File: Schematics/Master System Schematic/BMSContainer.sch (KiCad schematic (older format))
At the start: 2 parts, among them U1 OrionBMS2v2, U2 OrionThermExp

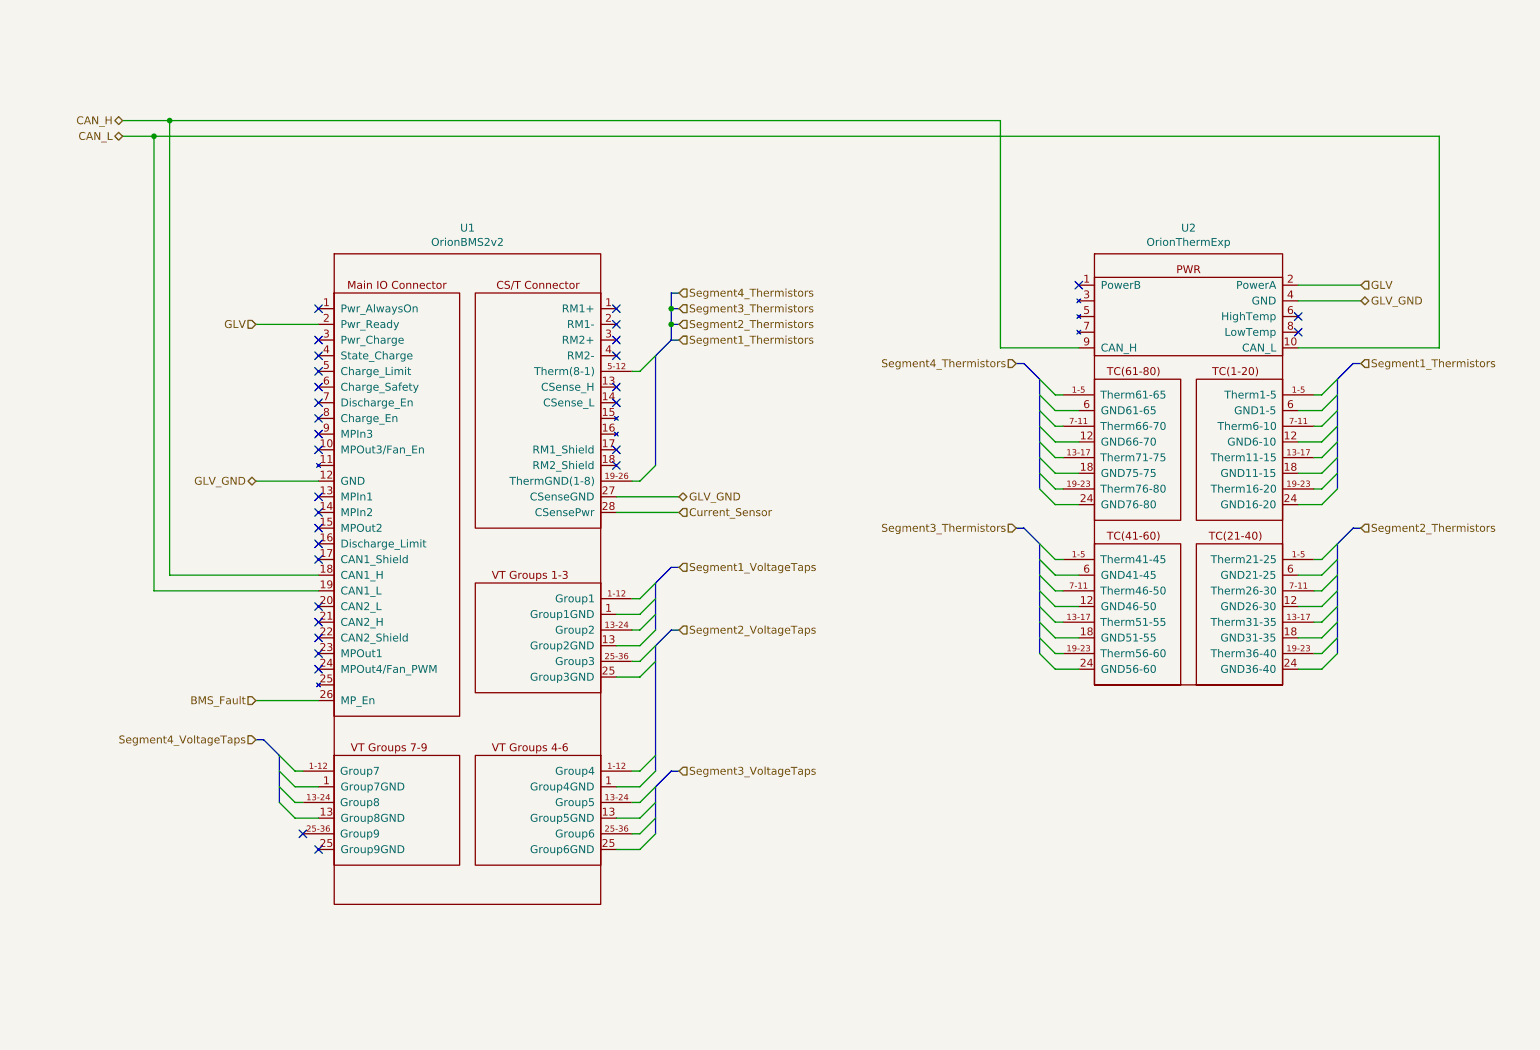
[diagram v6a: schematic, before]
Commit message: Additional corrections
>Moved GLV+ and GLV_GND pins to indicate single connections to enclosure
>Added charger safety line to charger
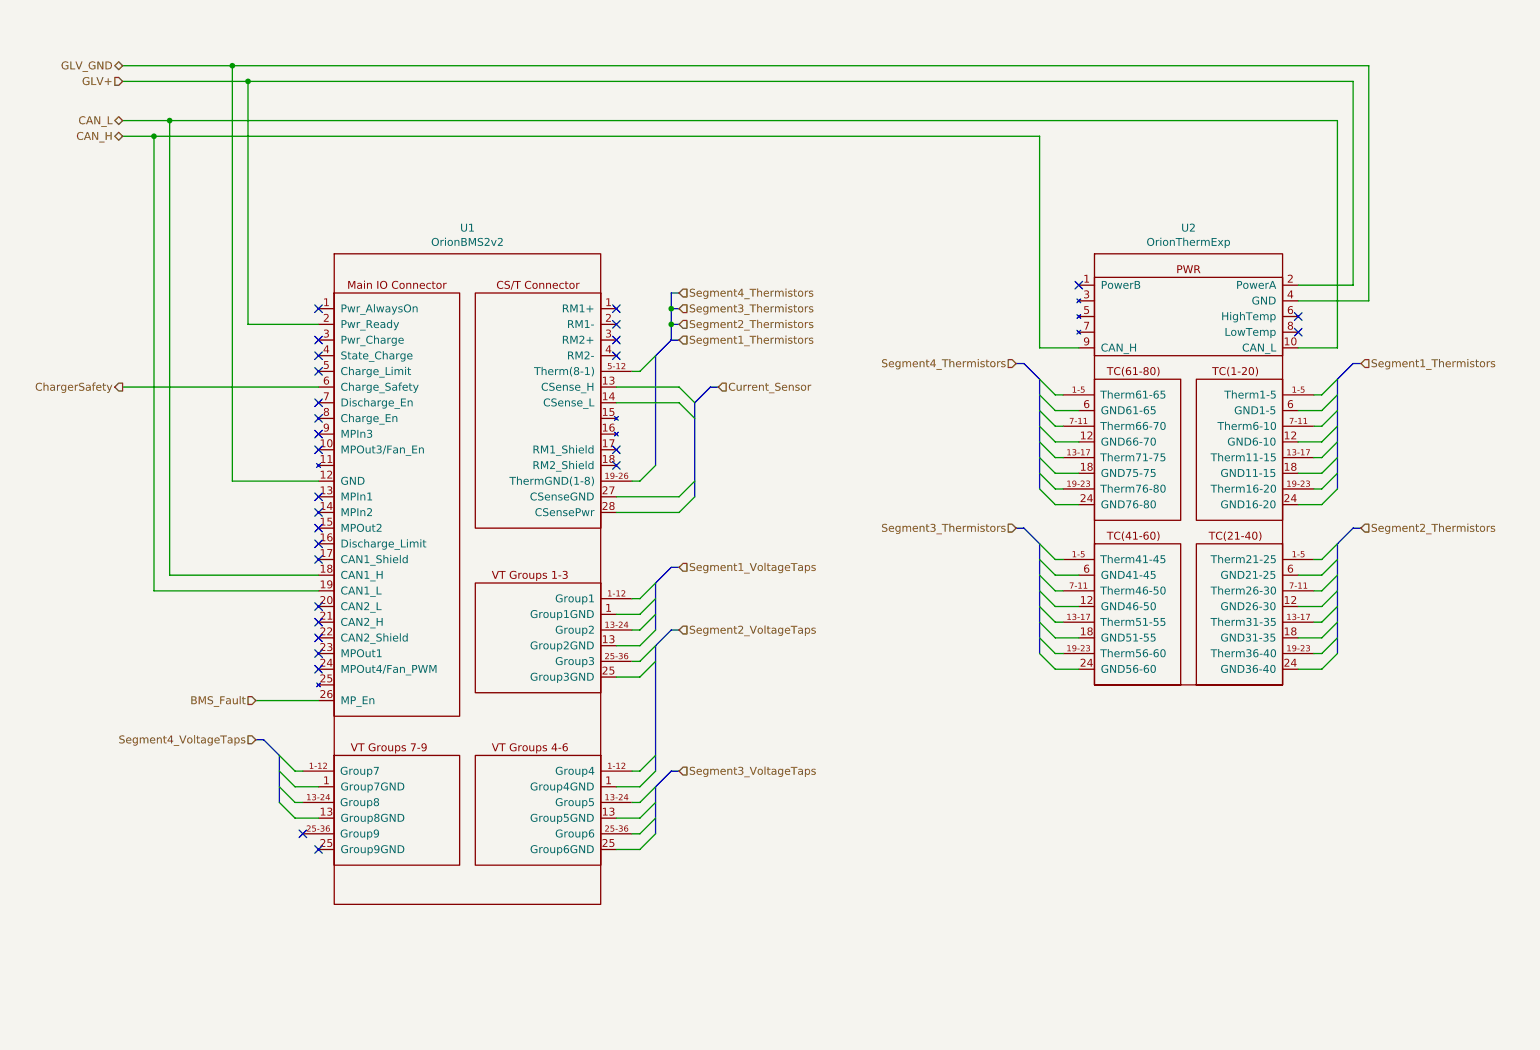
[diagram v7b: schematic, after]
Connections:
- net GLV is gone; now on net GLV+: U1.2 (RM1-), U2.2 (PowerA)
- net CAN_H: now also U1.19 (CAN1_L); no longer U1.18 (RM2_Shield)
- net CAN_L: now also U1.18 (RM2_Shield); no longer U1.19 (CAN1_L)
- net Current_Sensor: no longer U1.28 (CSensePwr)
- net GLV_GND: no longer U1.27 (CSenseGND)
- net GLV+: now reaches U1.2 (RM1-)
- net ChargerSafety: now reaches U1.6 (Charge_Safety)
- no-connect marks 32 -> 29
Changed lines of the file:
@@
 $Descr A 11000 8500
 encoding utf-8
-Sheet 1 1
+Sheet 4 17
 Title "BMS Container Schematic"
 Date "2020-10-16"
@@
 Text HLabel 6800 3650 0    50   Input ~ 0
 Segment3_Thermistors
+Text HLabel 1100 1150 0    50   BiDi ~ 0
+CAN_H
 Text HLabel 1100 1050 0    50   BiDi ~ 0
-CAN_H
-Text HLabel 1100 1150 0    50   BiDi ~ 0
 CAN_L
-Text HLabel 1950 2350 0    50   Input ~ 0
-GLV
-Text HLabel 1950 3350 0    50   BiDi ~ 0
+Text HLabel 1100 800  0    50   Input ~ 0
+GLV+
+Text HLabel 1100 700  0    50   BiDi ~ 0
 GLV_GND
 Text HLabel 1950 5000 0    50   Input ~ 0
@@
 Entry Bus Bus
 	8850 3750 8950 3650
-Text HLabel 9000 2200 2    50   BiDi ~ 0
-GLV_GND
 Text HLabel 1950 4750 0    50   Input ~ 0
 BMS_Fault
@@
 Wire Wire Line
 	8700 2800 8750 2800
-Wire Wire Line
-	9000 2200 8600 2200
-Text HLabel 9000 2100 2    50   Input ~ 0
-GLV
-Wire Wire Line
-	9000 2100 8600 2100
-$Comp
-L NER:OrionBMS2v2 U1
-U 1 1 5F91103C
-P 3300 3100
-F 0 "U1" H 3300 4465 50  0000 C CNN
-F 1 "OrionBMS2v2" H 3300 4374 50  0000 C CNN
-F 2 "" H 3300 4400 50  0001 C CNN
-F 3 "" H 3300 4400 50  0001 C CNN
-	1    3300 3100
-	1    0    0    -1
-$EndComp
-Text HLabel 4650 3550 2    50   Input ~ 0
+Text HLabel 4900 2750 2    50   Input ~ 0
 Current_Sensor
 Text HLabel 4650 5200 2    50   Input ~ 0
@@
 	2000 5000 1950 5000
 Wire Wire Line
-	1950 3350 2350 3350
-Wire Wire Line
-	1950 2350 2350 2350
-Text HLabel 4650 3450 2    50   BiDi ~ 0
-GLV_GND
-Wire Wire Line
 	4650 3450 4250 3450
-Wire Wire Line
-	4650 3550 4250 3550
 Entry Wire Line
 	4400 3350 4500 3250
@@
 Wire Wire Line
 	4350 3350 4400 3350
-Wire Bus Line
-	4500 2550 4500 3250
 Entry Bus Bus
 	4500 2550 4600 2450
@@
 NoConn ~ 2350 2550
 NoConn ~ 2350 2650
-NoConn ~ 2350 2750
 NoConn ~ 2350 2850
 NoConn ~ 2350 2950
@@
 	1300 4050 2350 4050
 Wire Wire Line
-	1400 1050 6700 1050
-Wire Wire Line
-	6700 1050 6700 2500
-Connection ~ 1400 1050
-Wire Wire Line
-	1300 1150 9500 1150
-Wire Wire Line
-	9500 1150 9500 2500
-Wire Wire Line
-	8600 2500 9500 2500
-Connection ~ 1300 1150
-Wire Wire Line
-	6700 2500 7200 2500
+	8600 2500 8850 2500
 Wire Wire Line
 	1400 3950 2350 3950
@@
 NoConn ~ 4250 2450
 NoConn ~ 4250 2550
-NoConn ~ 4250 2750
-NoConn ~ 4250 2850
 NoConn ~ 4250 3150
 NoConn ~ 4250 3250
 Wire Bus Line
+	4900 2750 4850 2750
+Entry Bus Bus
+	4850 2750 4750 2850
+Wire Bus Line
+	4500 2550 4500 3250
+$Comp
+L NER:OrionBMS2v2 U1
+U 1 1 5F91103C
+P 3300 3100
+F 0 "U1" H 3300 4465 50  0000 C CNN
+F 1 "OrionBMS2v2" H 3300 4374 50  0000 C CNN
+F 2 "" H 3300 4400 50  0001 C CNN
+F 3 "" H 3300 4400 50  0001 C CNN
+	1    3300 3100
+	1    0    0    -1
+$EndComp
+Wire Wire Line
+	4250 2850 4650 2850
+Wire Wire Line
+	4250 2750 4650 2750
+Wire Wire Line
+	4250 3550 4650 3550
+Entry Wire Line
+	4650 2750 4750 2850
+Entry Wire Line
+	4650 2850 4750 2950
+Entry Wire Line
+	4650 3450 4750 3350
+Entry Wire Line
+	4650 3550 4750 3450
+Wire Wire Line
+	1800 3350 2350 3350
+Wire Wire Line
+	1900 2350 2350 2350
+Wire Wire Line
+	9050 700  9050 2200
+Wire Wire Line
+	1100 800  1900 800
+Wire Wire Line
+	1100 700  1800 700
+Wire Wire Line
+	1900 2350 1900 800
+Connection ~ 1900 800
+Wire Wire Line
+	1800 3350 1800 700
+Connection ~ 1800 700
+Connection ~ 1300 1150
+Wire Wire Line
+	6950 1150 6950 2500
+Wire Wire Line
+	6950 2500 7200 2500
+Wire Wire Line
+	1300 1150 6950 1150
+Connection ~ 1400 1050
+Wire Wire Line
+	8850 1050 1400 1050
+Wire Wire Line
+	8850 1050 8850 2500
+Wire Wire Line
+	9050 2200 8600 2200
+Wire Wire Line
+	8600 2100 8950 2100
+Wire Wire Line
+	8950 800  8950 2100
+Wire Wire Line
+	1900 800  8950 800
+Wire Wire Line
+	1800 700  9050 700
+Text HLabel 1100 2750 0    50   Output ~ 0
+ChargerSafety
+Wire Wire Line
+	1100 2750 2350 2750
+Wire Bus Line
 	4500 4000 4500 4300
 Wire Bus Line
@@
 	2100 5100 2100 5400
 Wire Bus Line
+	4750 2850 4750 3450
+Wire Bus Line
 	8850 2700 8850 3400
